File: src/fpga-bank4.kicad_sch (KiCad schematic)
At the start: 1 part

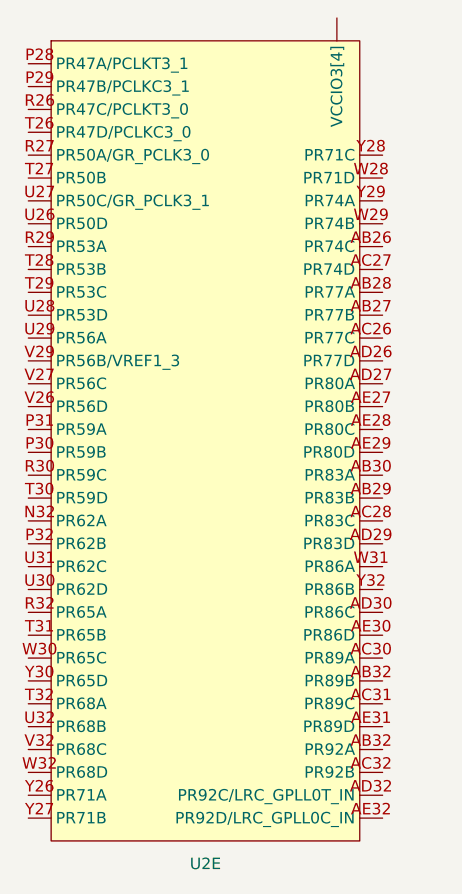
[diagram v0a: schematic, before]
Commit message: Finishes FPGA symbol
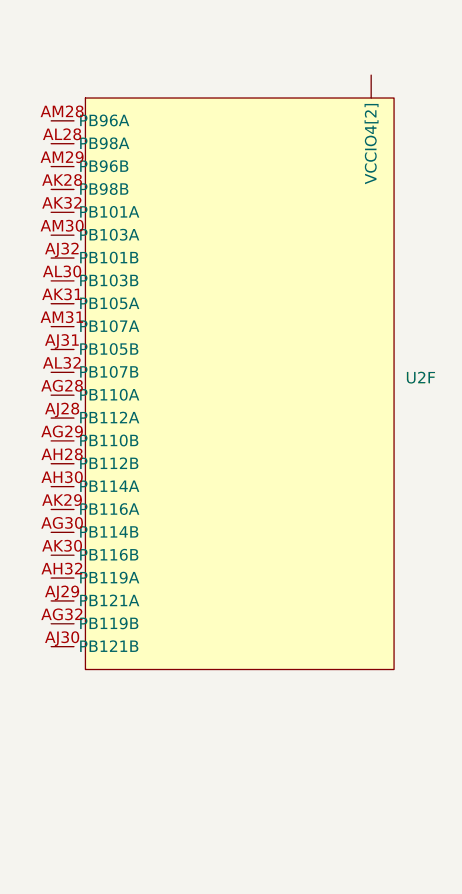
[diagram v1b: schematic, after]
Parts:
- removed U2: ~, symbol ECAP5-BSOM:LFE5U-85F-*BG756*
- added U2: ~, symbol ECAP5-BSOM:LFE5U-85F-*BG756*
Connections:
- new net VCCIO4: U2. (VCCIO4[2]), U2.AB23 (VCCIO4), U2.AC23 (VCCIO4)
